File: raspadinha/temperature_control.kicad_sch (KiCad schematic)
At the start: 7 parts, among them M1 Fan_CPU_4pin, Q1 IRF640N

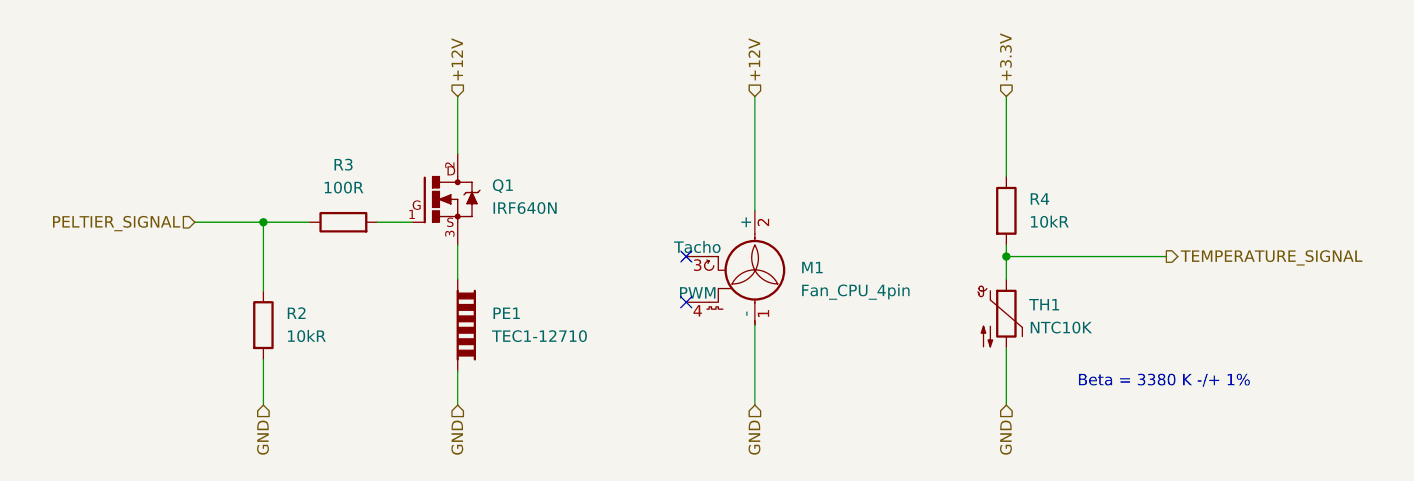
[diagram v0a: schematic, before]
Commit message: feat: usando o mosfet IRFZ44N feat: switch de on/off na fonte de alimentação
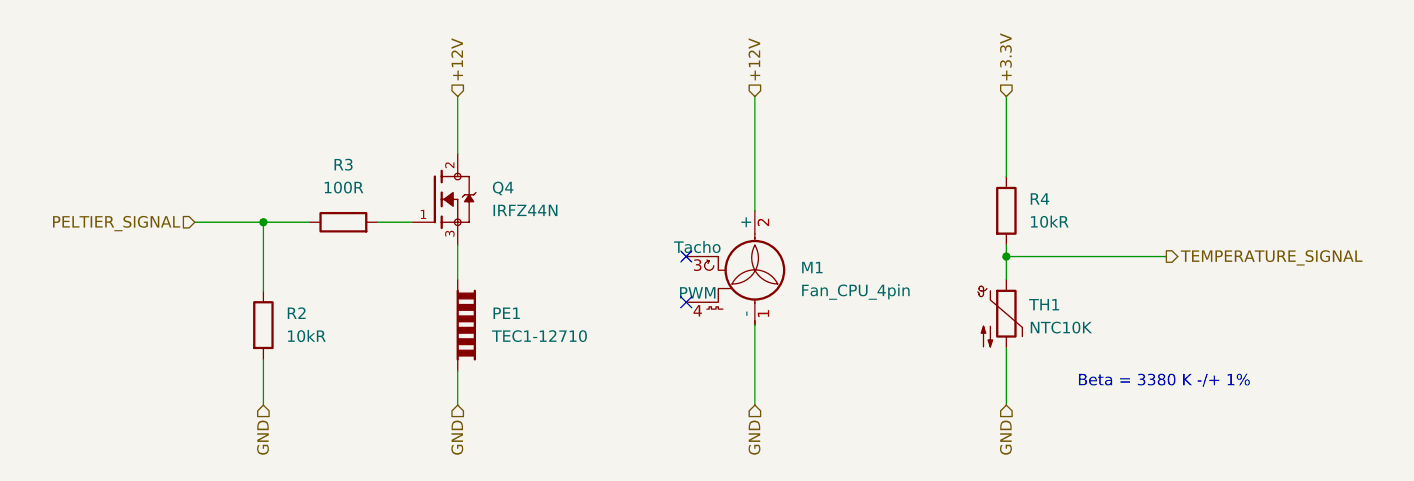
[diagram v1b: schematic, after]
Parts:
- removed Q1: IRF640N, symbol IRF640N:IRF640N
- added Q4: IRFZ44N, IRFZ44N:TO254P1016X419X2286-3, symbol IRFZ44N:IRFZ44N
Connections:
- net +12V: now also Q4.2
- net at R3.2: now also Q4.1
- net at PE1.1: now also Q4.3
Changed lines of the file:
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@@
 	)
 	(symbol
-		(lib_id "IRF640N:IRF640N")
+		(lib_id "IRFZ44N:IRFZ44N")
 		(at 120.65 87.63 0)
 		(unit 1)
@@
 		(dnp no)
 		(fields_autoplaced yes)
-		(property "Reference" "Q1"
-			(at 127 86.0977 0)
+		(property "Reference" "Q4"
+			(at 127 86.3599 0)
 			(effects
 				(font
@@
 			)
 		)
-		(property "Value" "IRF640N"
-			(at 127 88.6377 0)
+		(property "Value" "IRFZ44N"
+			(at 127 88.8999 0)
 			(effects
 				(font
@@
 			)
 		)
-		(property "Footprint" ""
+		(property "Footprint" "IRFZ44N:TO254P1016X419X2286-3"
 			(at 120.65 87.63 0)
 			(effects
@@
 					(size 1.27 1.27)
 				)
+				(justify bottom)
 				(hide yes)
 			)
@@
 			)
 		)
-		(property "Description_1" "N-Channel 200V 18A (Tc) 150W (Tc) Through Hole TO-220AB"
+		(property "MAXIMUM_PACKAGE_HEIGHT" "22.86 mm"
 			(at 120.65 87.63 0)
 			(effects
@@
 			)
 		)
-		(property "Package" "TO-263-3 Infineon Technologies"
+		(property "Package" "TO-220AB-3 Infineon"
 			(at 120.65 87.63 0)
 			(effects
@@
 			)
 		)
-		(property "SnapEDA_Link" "https://www.snapeda.com/parts/IRF640N/Infineon/view-part/?ref=snap"
+		(property "Check_prices" "https://www.snapeda.com/parts/IRFZ44N/Infineon/view-part/?ref=eda"
 			(at 120.65 87.63 0)
 			(effects
@@
 			)
 		)
-		(property "MP" "IRF640N"
+		(property "STANDARD" "IPC 7351B"
 			(at 120.65 87.63 0)
 			(effects
@@
 			)
 		)
-		(property "Availability" "Not in stock"
+		(property "PARTREV" "09/21/10"
 			(at 120.65 87.63 0)
 			(effects
@@
 			)
 		)
-		(property "Check_prices" "https://www.snapeda.com/parts/IRF640N/Infineon/view-part/?ref=eda"
+		(property "SnapEDA_Link" "https://www.snapeda.com/parts/IRFZ44N/Infineon/view-part/?ref=snap"
 			(at 120.65 87.63 0)
 			(effects
@@
 			)
 		)
-		(pin "3"
+		(property "MP" "IRFZ44N"
+			(at 120.65 87.63 0)
+			(effects
+				(font
+					(size 1.27 1.27)
+				)
+				(justify bottom)
+				(hide yes)
+			)
+		)
+		(property "Description_1" "N-Channel 55 V 49A (Tc) 94W (Tc) Through Hole TO-220AB"
+			(at 120.65 87.63 0)
+			(effects
+				(font
+					(size 1.27 1.27)
+				)
+				(justify bottom)
+				(hide yes)
+			)
+		)
+		(property "SNAPEDA_PN" "IRFZ44N"
+			(at 120.65 87.63 0)
+			(effects
+				(font
+					(size 1.27 1.27)
+				)
+				(justify bottom)
+				(hide yes)
+			)
+		)
+		(property "Availability" "In Stock"
+			(at 120.65 87.63 0)
+			(effects
+				(font
+					(size 1.27 1.27)
+				)
+				(justify bottom)
+				(hide yes)
+			)
+		)
+		(property "MANUFACTURER" "Infineon"
+			(at 120.65 87.63 0)
+			(effects
+				(font
+					(size 1.27 1.27)
+				)
+				(justify bottom)
+				(hide yes)
+			)
 		)
 		(pin "2"
+		)
+		(pin "3"
 		)
 		(pin "1"
 		)
 		(instances
-			(project "raspadinha"
+			(project ""
 				(path "/0ce4bf39-76b0-428c-8682-47e2500753cc/c4af42a8-46c6-40b9-a84b-e5efe0664160"
-					(reference "Q1")
+					(reference "Q4")
 					(unit 1)
 				)

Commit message: feat: Os Footprint foram todos atribuidos fix: A placa da Esp32 foi trocada pela que temos disponível
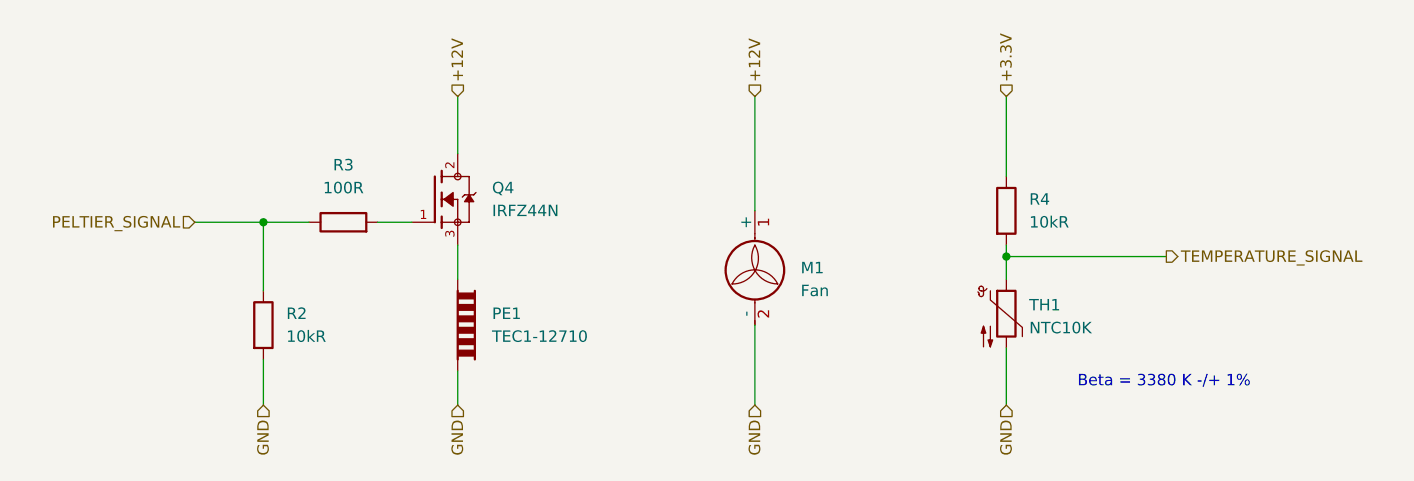
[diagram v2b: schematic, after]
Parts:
- removed M1: Fan_CPU_4pin, symbol Motor:Fan_CPU_4pin
- added M1: Fan, Connector_Molex:Molex_KK-254_AE-6410-02A_1x02_P2.54mm_Vertical, symbol Motor:Fan
- PE1: footprint (none) -> TerminalBlock_Phoenix:TerminalBlock_Phoenix_PT-1,5-2-3.5-H_1x02_P3.50mm_Horizontal
- R2, R3, R4: footprint (none) -> Resistor_THT:R_Axial_DIN0411_L9.9mm_D3.6mm_P12.70mm_Horizontal
- TH1: footprint (none) -> Connector_Molex:Molex_KK-254_AE-6410-02A_1x02_P2.54mm_Vertical
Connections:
- net +12V: now also M1.1 (+)
- net GND: now also M1.2 (-)
- no-connect marks 2 -> 0
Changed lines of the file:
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@@
 		(title "Geladinho, Temperature control")
 		(date "2025-11-20")
-		(rev "v1.0.0")
+		(rev "v1.1.0")
 		(company "Universidade Federal Do Ceará")
 	)
@@
 		(color 0 0 0 0)
 	)
-	(no_connect
-		(at 148.59 93.98)
-	)
-	(no_connect
-		(at 148.59 99.06)
-	)
 	(wire
 		(pts
@@
 			)
 			(justify left)
-		)
-	)
-	(symbol
-		(lib_id "Motor:Fan_CPU_4pin")
-		(at 156.21 96.52 0)
-		(unit 1)
-		(exclude_from_sim no)
-		(in_bom yes)
-		(on_board yes)
-		(dnp no)
-		(fields_autoplaced yes)
-		(property "Reference" "M1"
-			(at 161.29 95.2499 0)
-			(effects
-				(font
-					(size 1.27 1.27)
-				)
-				(justify left)
-			)
-		)
-		(property "Value" "Fan_CPU_4pin"
-			(at 161.29 97.7899 0)
-			(effects
-				(font
-					(size 1.27 1.27)
-				)
-				(justify left)
-			)
-		)
-		(property "Footprint" ""
-			(at 156.21 96.266 0)
-			(effects
-				(font
-					(size 1.27 1.27)
-				)
-				(hide yes)
-			)
-		)
-		(property "Datasheet" "http://www.formfactors.org/developer%5Cspecs%5Crev1_2_public.pdf"
-			(at 156.21 96.266 0)
-			(effects
-				(font
-					(size 1.27 1.27)
-				)
-				(hide yes)
-			)
-		)
-		(property "Description" "CPU Fan, tacho output, PWM input, 4-pin connector"
-			(at 156.21 96.52 0)
-			(effects
-				(font
-					(size 1.27 1.27)
-				)
-				(hide yes)
-			)
-		)
-		(pin "3"
-		)
-		(pin "4"
-		)
-		(pin "2"
-		)
-		(pin "1"
-		)
-		(instances
-			(project "raspadinha"
-				(path "/0ce4bf39-76b0-428c-8682-47e2500753cc/c4af42a8-46c6-40b9-a84b-e5efe0664160"
-					(reference "M1")
-					(unit 1)
-				)
-			)
 		)
 	)
@@
 			)
 		)
-		(property "Footprint" ""
+		(property "Footprint" "Resistor_THT:R_Axial_DIN0411_L9.9mm_D3.6mm_P12.70mm_Horizontal"
 			(at 182.372 88.9 90)
 			(effects
@@
 			)
 		)
-		(property "Footprint" ""
+		(property "Footprint" "Resistor_THT:R_Axial_DIN0411_L9.9mm_D3.6mm_P12.70mm_Horizontal"
 			(at 110.49 91.948 90)
 			(effects
@@
 			)
 		)
-		(property "Footprint" ""
+		(property "Footprint" "Connector_Molex:Molex_KK-254_AE-6410-02A_1x02_P2.54mm_Vertical"
 			(at 184.15 99.06 0)
 			(effects
@@
 				(path "/0ce4bf39-76b0-428c-8682-47e2500753cc/c4af42a8-46c6-40b9-a84b-e5efe0664160"
 					(reference "TH1")
+					(unit 1)
+				)
+			)
+		)
+	)
+	(symbol
+		(lib_id "Motor:Fan")
+		(at 156.21 96.52 0)
+		(unit 1)
+		(exclude_from_sim no)
+		(in_bom yes)
+		(on_board yes)
+		(dnp no)
+		(fields_autoplaced yes)
+		(property "Reference" "M1"
+			(at 161.29 95.2499 0)
+			(effects
+				(font
+					(size 1.27 1.27)
+				)
+				(justify left)
+			)
+		)
+		(property "Value" "Fan"
+			(at 161.29 97.7899 0)
+			(effects
+				(font
+					(size 1.27 1.27)
+				)
+				(justify left)
+			)
+		)
+		(property "Footprint" "Connector_Molex:Molex_KK-254_AE-6410-02A_1x02_P2.54mm_Vertical"
+			(at 156.21 96.266 0)
+			(effects
+				(font
+					(size 1.27 1.27)
+				)
+				(hide yes)
+			)
+		)
+		(property "Datasheet" "~"
+			(at 156.21 96.266 0)
+			(effects
+				(font
+					(size 1.27 1.27)
+				)
+				(hide yes)
+			)
+		)
+		(property "Description" "Fan"
+			(at 156.21 96.52 0)
+			(effects
+				(font
+					(size 1.27 1.27)
+				)
+				(hide yes)
+			)
+		)
+		(pin "2"
+		)
+		(pin "1"
+		)
+		(instances
+			(project ""
+				(path "/0ce4bf39-76b0-428c-8682-47e2500753cc/c4af42a8-46c6-40b9-a84b-e5efe0664160"
+					(reference "M1")
 					(unit 1)
 				)
@@
 			)
 		)
-		(property "Footprint" ""
+		(property "Footprint" "TerminalBlock_Phoenix:TerminalBlock_Phoenix_PT-1,5-2-3.5-H_1x02_P3.50mm_Horizontal"
 			(at 121.412 101.6 0)
 			(effects
@@
 			)
 		)
-		(property "Footprint" ""
+		(property "Footprint" "Resistor_THT:R_Axial_DIN0411_L9.9mm_D3.6mm_P12.70mm_Horizontal"
 			(at 99.822 101.6 90)
 			(effects

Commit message: feat: Refatoração da alimentação da placa feat: Renomeação do número dos componentes
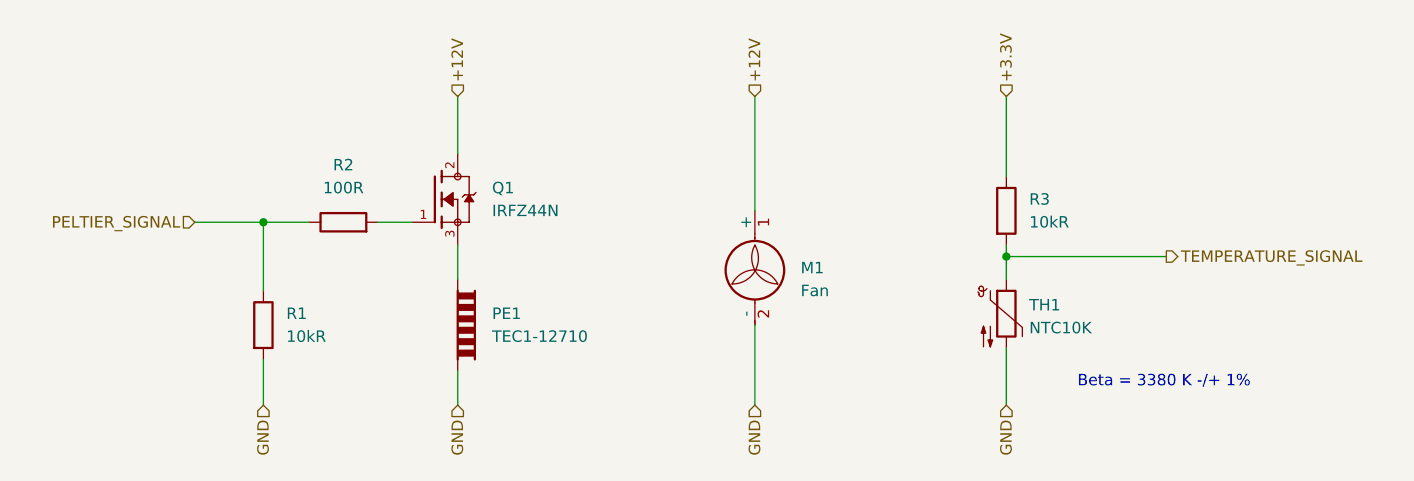
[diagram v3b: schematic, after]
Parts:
- renumbered Q4 to Q1, R2 to R1, R3 to R2, R4 to R3
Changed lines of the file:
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@@
 		(dnp no)
 		(fields_autoplaced yes)
-		(property "Reference" "Q4"
+		(property "Reference" "Q1"
 			(at 127 86.3599 0)
 			(effects
@@
 			(project ""
 				(path "/0ce4bf39-76b0-428c-8682-47e2500753cc/c4af42a8-46c6-40b9-a84b-e5efe0664160"
-					(reference "Q4")
+					(reference "Q1")
 					(unit 1)
 				)
@@
 		(dnp no)
 		(fields_autoplaced yes)
-		(property "Reference" "R4"
+		(property "Reference" "R3"
 			(at 186.69 87.6299 0)
 			(effects
@@
 			(project "raspadinha"
 				(path "/0ce4bf39-76b0-428c-8682-47e2500753cc/c4af42a8-46c6-40b9-a84b-e5efe0664160"
-					(reference "R4")
+					(reference "R3")
 					(unit 1)
 				)
@@
 		(dnp no)
 		(fields_autoplaced yes)
-		(property "Reference" "R3"
+		(property "Reference" "R2"
 			(at 110.49 83.82 90)
 			(effects
@@
 			(project "raspadinha"
 				(path "/0ce4bf39-76b0-428c-8682-47e2500753cc/c4af42a8-46c6-40b9-a84b-e5efe0664160"
-					(reference "R3")
+					(reference "R2")
 					(unit 1)
 				)
@@
 		(dnp no)
 		(fields_autoplaced yes)
-		(property "Reference" "R2"
+		(property "Reference" "R1"
 			(at 104.14 100.3299 0)
 			(effects
@@
 			(project "raspadinha"
 				(path "/0ce4bf39-76b0-428c-8682-47e2500753cc/c4af42a8-46c6-40b9-a84b-e5efe0664160"
-					(reference "R2")
-					(unit 1)
-				)
+					(reference "R1")
+					(unit 1)
+				)
